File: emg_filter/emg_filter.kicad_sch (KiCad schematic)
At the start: 16 parts, among them U1 INA331

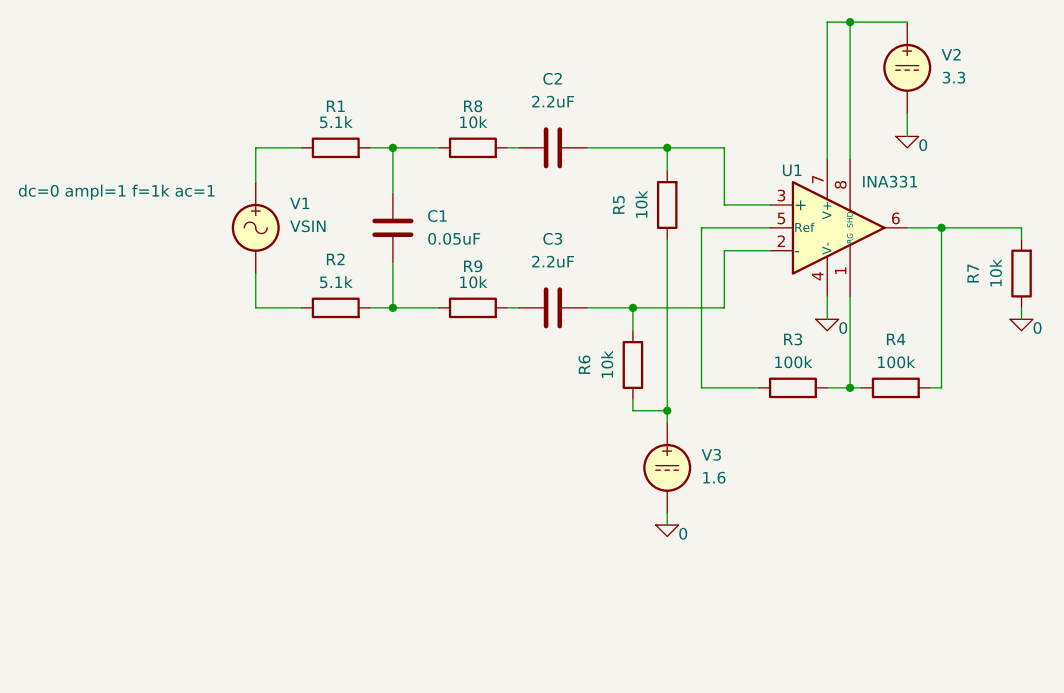
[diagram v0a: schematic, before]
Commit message: dif signal filter updated
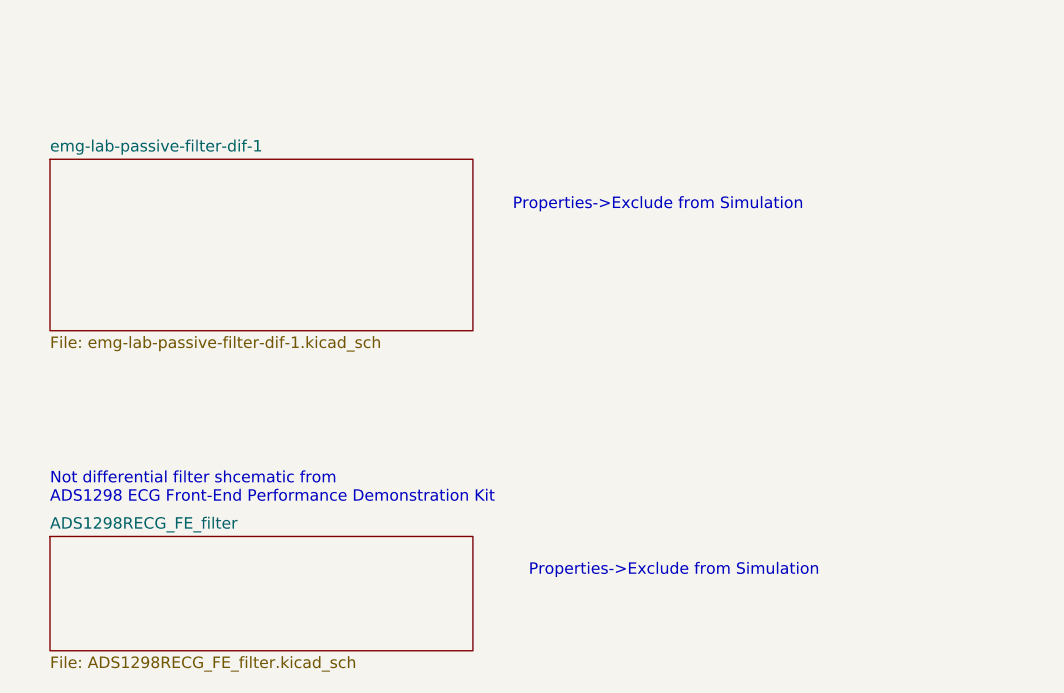
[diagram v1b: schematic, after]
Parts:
- removed C1: 0.05uF, symbol Device:C
- removed C2, C3: 2.2uF, symbol Device:C
- removed R1, R2: 5.1k, symbol Device:R
- removed R3, R4: 100k, symbol Device:R
- removed R5, R6, R7, R8, R9: 10k, symbol Device:R
- removed U1: INA331, symbol simulate-rescue:INA331-Amplifier_Instrumentation
- removed V1: VSIN, symbol Simulation_SPICE:VSIN
- removed V2: 3.3, symbol Simulation_SPICE:VDC
- removed V3: 1.6, symbol Simulation_SPICE:VDC
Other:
- added sheet ADS1298RECG_FE_filter (ADS1298RECG_FE_filter.kicad_sch)
- added sheet emg-lab-passive-filter-dif-1 (emg-lab-passive-filter-dif-1.kicad_sch)
- note added: "Not differential filter shcematic from ADS1298 ECG Front-End Performance Demonstration Kit"
- note added: "Properties->Exclude from Simulation"
